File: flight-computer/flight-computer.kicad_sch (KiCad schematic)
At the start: 42 parts, among them J1 Screw_Terminal_01x02, J2 Screw_Terminal_01x02, U1 MPU6050, U2 BMP180, U3 ESP32_DEVKIT, U4 W25Q64FV_Winbond_Flash_Memory, U5 MPU6050, U6 W25Q64FV_Winbond_Flash_Memory, U7 MPU6050, U8 BMP180, U9 BMP180

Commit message: added NEO6M GPS footprint
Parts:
- added U10: GPS-NEO6M, custom-footprints:GPS-NEO6M, symbol modules:GPS-NEO6M
- gave numbers to parts that had none: 2
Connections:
- net +5V: now also U10.1 (VCC)
- net GND: now also U10.4 (GND)
- net GPS_TX: now reaches U3.29 (RX2)
- net GPS_TX: now also U10.3 (TX)
- net GPS_RX: now reaches U3.30 (TX2)
- net GPS_RX: now also U10.2 (RX)
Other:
- note added: "GPS Module"
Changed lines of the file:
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@@
     (stroke (width 0) (type default) (color 0 0 0 0))
   )
-  (polyline (pts (xy 130.175 145.415) (xy 130.175 38.735))
+  (polyline (pts (xy 130.175 118.745) (xy 130.175 56.515))
     (stroke (width 0) (type default) (color 0 0 0 0))
   )
@@
     (stroke (width 0) (type default) (color 0 0 0 0))
   )
+  (polyline (pts (xy 205.105 153.67) (xy 130.175 153.67))
+    (stroke (width 0) (type default) (color 0 0 0 0))
+  )
+  (wire (pts (xy 139.065 130.81) (xy 139.065 131.445))
+    (stroke (width 0) (type default) (color 0 0 0 0))
+  )
   (wire (pts (xy 43.18 165.1) (xy 57.785 165.1))
     (stroke (width 0) (type default) (color 0 0 0 0))
@@
     (stroke (width 0) (type default) (color 0 0 0 0))
   )
-  (polyline (pts (xy 205.74 38.735) (xy 130.175 38.735))
+  (polyline (pts (xy 205.74 56.515) (xy 130.175 56.515))
     (stroke (width 0) (type default) (color 0 0 0 0))
   )
@@
     (stroke (width 0) (type default) (color 0 0 0 0))
   )
-  (polyline (pts (xy 205.74 145.415) (xy 130.175 145.415))
+  (polyline (pts (xy 205.74 118.745) (xy 130.175 118.745))
     (stroke (width 0) (type default) (color 0 0 0 0))
   )
@@
     (stroke (width 0) (type default) (color 0 0 0 0))
   )
+  (polyline (pts (xy 205.105 123.19) (xy 205.105 153.67))
+    (stroke (width 0) (type default) (color 0 0 0 0))
+  )
   (wire (pts (xy 44.45 113.03) (xy 58.42 113.03))
     (stroke (width 0) (type default) (color 0 0 0 0))
   )
+  (polyline (pts (xy 130.175 123.19) (xy 130.175 153.67))
+    (stroke (width 0) (type default) (color 0 0 0 0))
+  )
   (wire (pts (xy 237.49 21.59) (xy 237.49 24.13))
     (stroke (width 0) (type default) (color 0 0 0 0))
@@
     (stroke (width 0) (type default) (color 0 0 0 0))
   )
+  (wire (pts (xy 159.385 130.81) (xy 139.065 130.81))
+    (stroke (width 0) (type default) (color 0 0 0 0))
+  )
   (polyline (pts (xy 127 153.035) (xy 127 105.41))
     (stroke (width 0) (type default) (color 0 0 0 0))
@@
     (stroke (width 0) (type default) (color 0 0 0 0))
   )
+  (wire (pts (xy 158.75 138.43) (xy 159.385 138.43))
+    (stroke (width 0) (type default) (color 0 0 0 0))
+  )
   (wire (pts (xy 40.005 33.655) (xy 40.005 38.1))
     (stroke (width 0) (type default) (color 0 0 0 0))
@@
     (stroke (width 0) (type default) (color 0 0 0 0))
   )
+  (polyline (pts (xy 130.175 123.19) (xy 205.105 123.19))
+    (stroke (width 0) (type default) (color 0 0 0 0))
+  )
   (wire (pts (xy 97.79 165.1) (xy 112.395 165.1))
     (stroke (width 0) (type default) (color 0 0 0 0))
@@
     (stroke (width 0) (type default) (color 0 0 0 0))
   )
-  (polyline (pts (xy 205.74 38.735) (xy 205.74 145.415))
+  (polyline (pts (xy 205.74 56.515) (xy 205.74 118.745))
     (stroke (width 0) (type default) (color 0 0 0 0))
   )
@@
     (stroke (width 0) (type default) (color 0 0 0 0))
   )
-  (text "MCU\n" (at 130.81 41.275 0)
+  (text "MCU\n" (at 130.81 59.69 0)
     (effects (font (size 1.27 1.27) bold) (justify left bottom))
   )
@@
     (at 76.2 109.855 0)
     (effects (font (size 1.27 1.27)) (justify left bottom))
+  )
+  (text "GPS Module" (at 130.81 125.73 0)
+    (effects (font (size 1.27 1.27) bold) (justify left bottom))
   )
   (text "Address: 0X77" (at 57.785 158.75 0)
@@
     )
   )
+  (global_label "GPS_RX" (shape input) (at 159.385 135.89 180) (fields_autoplaced)
+    (effects (font (size 1.27 1.27) bold) (justify right))
+    (property "Intersheet References" "${INTERSHEET_REFS}" (id 0) (at 149.5848 136.017 0)
+      (effects (font (size 1.27 1.27) bold) (justify right) hide)
+    )
+  )
   (global_label "~{HOLD}" (shape input) (at 247.65 57.15 0) (fields_autoplaced)
     (effects (font (size 1.27 1.27) bold) (justify left))
@@
     )
   )
+  (global_label "GPS_TX" (shape input) (at 186.055 90.805 0) (fields_autoplaced)
+    (effects (font (size 1.27 1.27) bold) (justify left))
+    (property "Intersheet References" "${INTERSHEET_REFS}" (id 0) (at 195.5528 90.932 0)
+      (effects (font (size 1.27 1.27) bold) (justify left) hide)
+    )
+  )
   (global_label "SDA" (shape input) (at 39.37 119.38 90) (fields_autoplaced)
     (effects (font (size 1.27 1.27)) (justify left))
@@
     )
   )
+  (global_label "GPS_TX" (shape input) (at 159.385 133.35 180) (fields_autoplaced)
+    (effects (font (size 1.27 1.27) bold) (justify right))
+    (property "Intersheet References" "${INTERSHEET_REFS}" (id 0) (at 149.8872 133.223 0)
+      (effects (font (size 1.27 1.27) bold) (justify right) hide)
+    )
+  )
   (global_label "D0" (shape input) (at 223.52 57.15 180) (fields_autoplaced)
     (effects (font (size 1.27 1.27) bold) (justify right))
@@
     (effects (font (size 1.27 1.27) bold) (justify left))
     (property "Intersheet References" "${INTERSHEET_REFS}" (id 0) (at 253.8216 60.833 0)
+      (effects (font (size 1.27 1.27) bold) (justify left) hide)
+    )
+  )
+  (global_label "GPS_RX" (shape input) (at 186.055 88.265 0) (fields_autoplaced)
+    (effects (font (size 1.27 1.27) bold) (justify left))
+    (property "Intersheet References" "${INTERSHEET_REFS}" (id 0) (at 195.8552 88.138 0)
       (effects (font (size 1.27 1.27) bold) (justify left) hide)
     )
@@
   (symbol (lib_id "power:GND") (at 62.865 47.625 0) (unit 1)
     (in_bom yes) (on_board yes)
-    (property "Reference" "#PWR?" (id 0) (at 62.865 53.975 0)
+    (property "Reference" "#PWR0141" (id 0) (at 62.865 53.975 0)
       (effects (font (size 1.27 1.27)) hide)
     )
@@
     )
     (property "Datasheet" "" (id 3) (at 62.865 47.625 0)
+      (effects (font (size 1.27 1.27)) hide)
+    )
+    (pin "1")
+  )
+  (symbol (lib_id "power:+5V") (at 158.75 138.43 90) (unit 1)
+    (in_bom yes) (on_board yes)
+    (property "Reference" "#PWR010" (id 0) (at 162.56 138.43 0)
+      (effects (font (size 1.27 1.27)) hide)
+    )
+    (property "Value" "+5V" (id 1) (at 151.765 138.43 90)
+      (effects (font (size 1.27 1.27)) (justify right))
+    )
+    (property "Footprint" "" (id 2) (at 158.75 138.43 0)
+      (effects (font (size 1.27 1.27)) hide)
+    )
+    (property "Datasheet" "" (id 3) (at 158.75 138.43 0)
       (effects (font (size 1.27 1.27)) hide)
     )
@@
     (pin "1")
   )
+  (symbol (lib_id "modules:GPS-NEO6M") (at 161.925 127 0) (unit 1)
+    (in_bom yes) (on_board yes) (fields_autoplaced)
+    (property "Reference" "U10" (id 0) (at 188.595 133.9849 0)
+      (effects (font (size 1.27 1.27)) (justify left))
+    )
+    (property "Value" "GPS-NEO6M" (id 1) (at 188.595 136.5249 0)
+      (effects (font (size 1.27 1.27)) (justify left))
+    )
+    (property "Footprint" "custom-footprints:GPS-NEO6M" (id 2) (at 168.275 125.73 0)
+      (effects (font (size 1.27 1.27)) hide)
+    )
+    (property "Datasheet" "" (id 3) (at 168.275 125.73 0)
+      (effects (font (size 1.27 1.27)) hide)
+    )
+    (pin "1")
+    (pin "2")
+    (pin "3")
+    (pin "4")
+  )
   (symbol (lib_id "power:GND") (at 261.62 66.04 0) (unit 1)
     (in_bom yes) (on_board yes)
@@
   (symbol (lib_id "Device:R") (at 62.865 43.815 0) (unit 1)
     (in_bom yes) (on_board yes) (fields_autoplaced)
-    (property "Reference" "R?" (id 0) (at 64.77 42.5449 0)
+    (property "Reference" "R1" (id 0) (at 64.77 42.5449 0)
       (effects (font (size 1.27 1.27)) (justify left))
     )
@@
   (symbol (lib_id "Device:LED") (at 62.865 36.195 90) (unit 1)
     (in_bom yes) (on_board yes) (fields_autoplaced)
-    (property "Reference" "D?" (id 0) (at 66.04 36.5124 90)
+    (property "Reference" "D2" (id 0) (at 66.04 36.5124 90)
       (effects (font (size 1.27 1.27)) (justify right))
     )
@@
     (pin "1")
   )
+  (symbol (lib_id "power:GND") (at 139.065 131.445 0) (unit 1)
+    (in_bom yes) (on_board yes)
+    (property "Reference" "#PWR09" (id 0) (at 139.065 137.795 0)
+      (effects (font (size 1.27 1.27)) hide)
+    )
+    (property "Value" "GND" (id 1) (at 138.43 135.89 0))
+    (property "Footprint" "" (id 2) (at 139.065 131.445 0)
+      (effects (font (size 1.27 1.27)) hide)
+    )
+    (property "Datasheet" "" (id 3) (at 139.065 131.445 0)
+      (effects (font (size 1.27 1.27)) hide)
+    )
+    (pin "1")
+  )
   (symbol (lib_id "toggle-switch:100SP1T1B4M2QE") (at 48.26 31.115 0) (unit 1)
     (in_bom yes) (on_board yes) (fields_autoplaced)
@@
       (reference "#PWR08") (unit 1) (value "GND") (footprint "")
     )
+    (path "/c8c902c7-0ab4-48a4-a0a1-d40b6bf4a2d5"
+      (reference "#PWR09") (unit 1) (value "GND") (footprint "")
+    )
+    (path "/2b471a04-e055-4567-a502-ae2af7a721d1"
+      (reference "#PWR010") (unit 1) (value "+5V") (footprint "")
+    )
     (path "/4fb3bb21-cae0-4e69-9248-759f3524059c"
       (reference "#PWR0101") (unit 1) (value "GND") (footprint "")
@@
     )
     (path "/23c0bb96-3ff8-4937-a107-4f0715059131"
-      (reference "#PWR?") (unit 1) (value "GND") (footprint "")
+      (reference "#PWR0141") (unit 1) (value "GND") (footprint "")
     )
     (path "/2dae9a2c-6370-4b32-88be-85d2eb9d4c00"
@@
     )
     (path "/68b26feb-598c-4a44-98ca-ad2ff34adbc9"
-      (reference "D?") (unit 1) (value "LED") (footprint "LED_SMD:LED_0805_2012Metric")
+      (reference "D2") (unit 1) (value "LED") (footprint "LED_SMD:LED_0805_2012Metric")
     )
     (path "/1936f0f3-1085-45ad-b499-8407ccaff28d"
@@
     )
     (path "/50759d54-4560-42cd-adb6-a64ce252b529"
-      (reference "R?") (unit 1) (value "R") (footprint "Resistor_SMD:R_0805_2012Metric")
+      (reference "R1") (unit 1) (value "R") (footprint "Resistor_SMD:R_0805_2012Metric")
     )
     (path "/cf0203bf-410f-4e09-a470-8e92c82dea6c"
@@
       (reference "U9") (unit 1) (value "BMP180") (footprint "custom-footprints:BMP180")
     )
-  )
+    (path "/4846449d-5e6e-4ab2-965e-226ba08fbd54"
+      (reference "U10") (unit 1) (value "GPS-NEO6M") (footprint "custom-footprints:GPS-NEO6M")
+    )
+  )

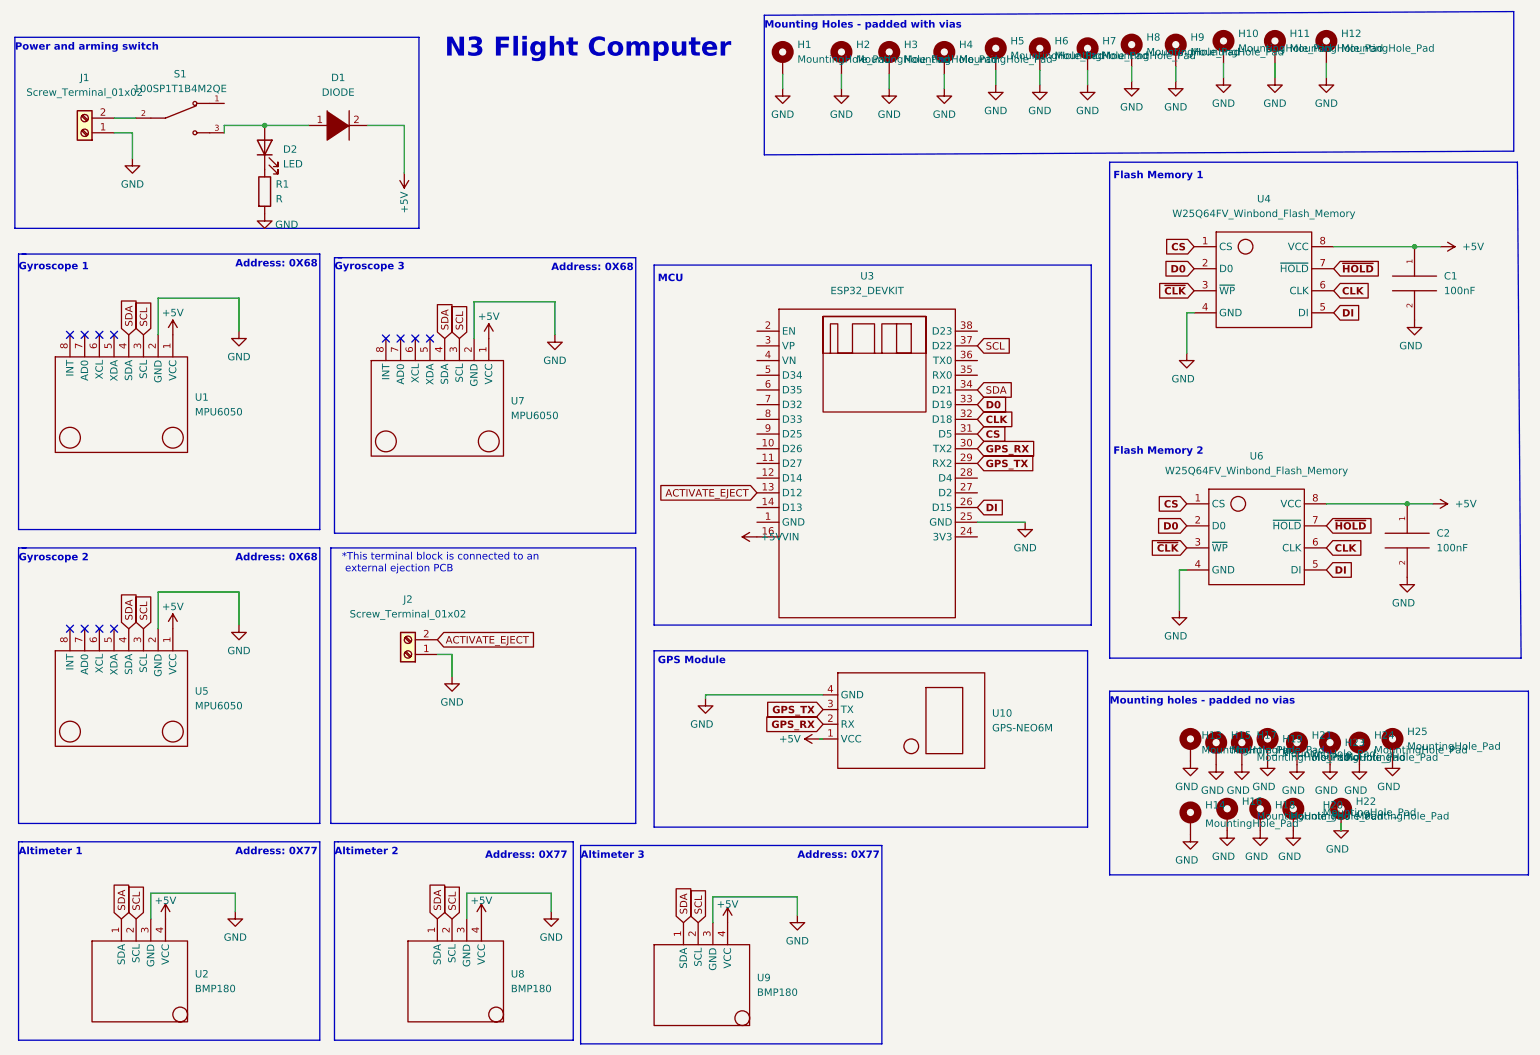
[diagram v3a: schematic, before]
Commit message: added pcb pdfs
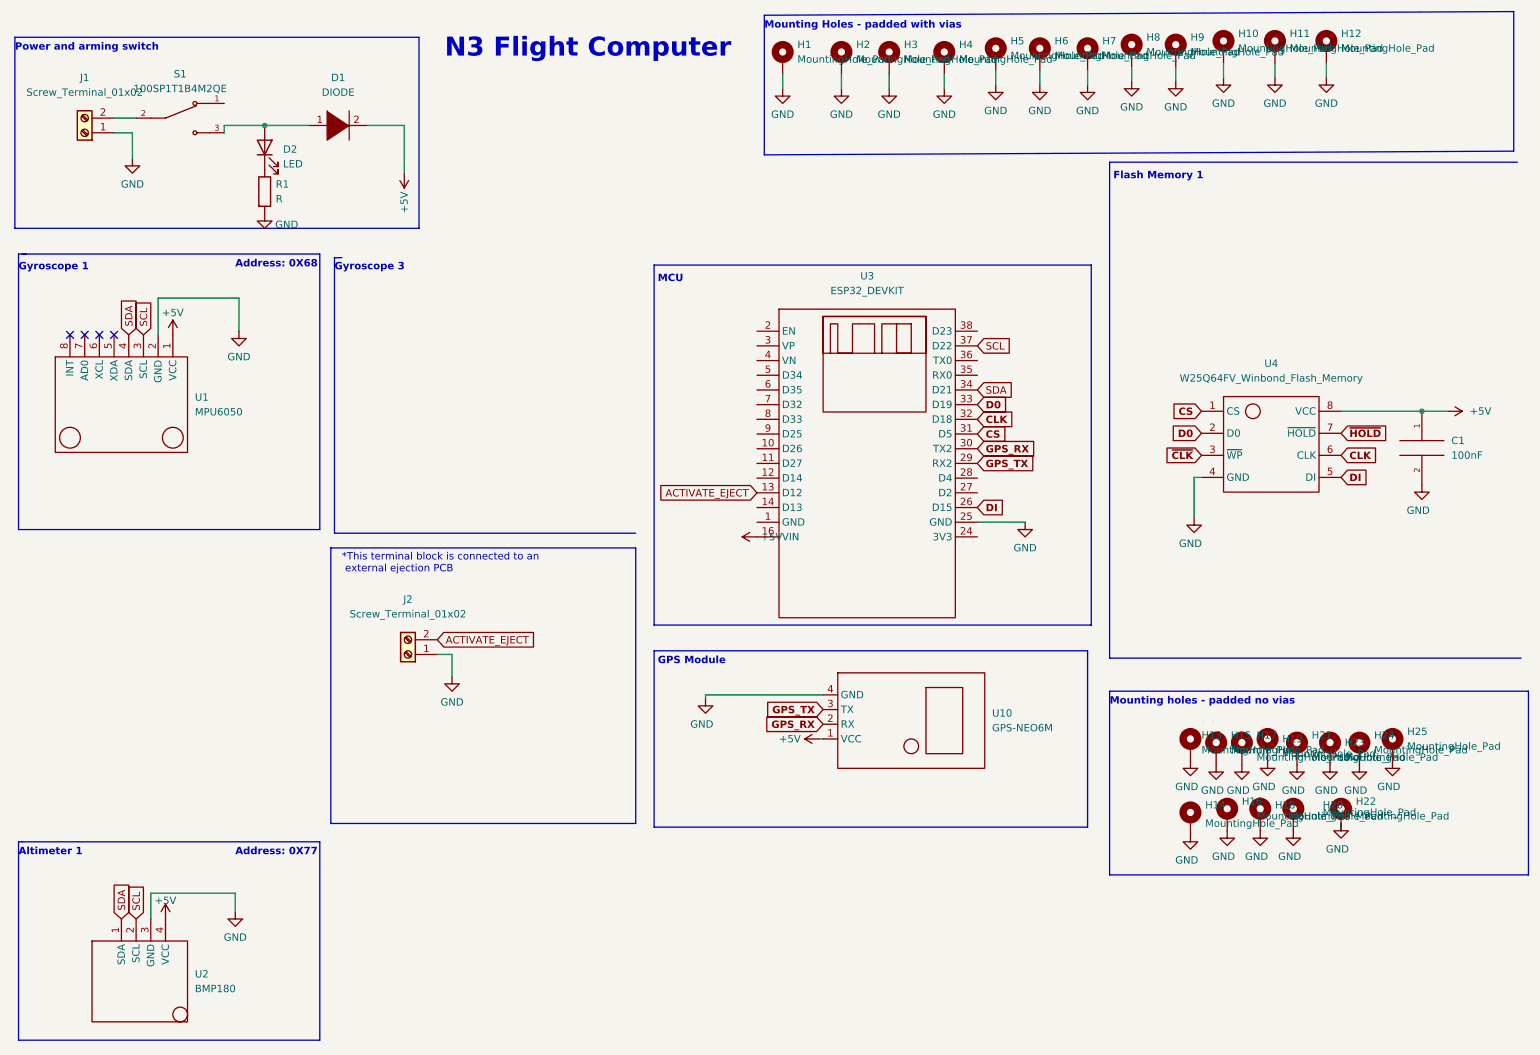
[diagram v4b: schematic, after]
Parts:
- removed C2: 100nF, Capacitor_SMD:C_0805_2012Metric, symbol pspice:CAP
- removed U5, U7: MPU6050, custom-footprints:MPU6050, symbol modules:MPU6050
- removed U6: W25Q64FV_Winbond_Flash_Memory, Package_SO:HTSOP-8-1EP_3.9x4.9mm_P1.27mm_EP2.4x3.2mm, symbol modules:W25Q64FV_Winbond_Flash_Memory
- removed U8, U9: BMP180, custom-footprints:BMP180, symbol modules:BMP180
- C1: footprint Capacitor_SMD:C_0805_2012Metric -> Capacitor_THT:CP_Radial_D4.0mm_P1.50mm
- D2: footprint LED_SMD:LED_0805_2012Metric -> LED_THT:LED_D3.0mm
- R1: footprint Resistor_SMD:R_0805_2012Metric -> Resistor_THT:R_Axial_DIN0204_L3.6mm_D1.6mm_P7.62mm_Horizontal
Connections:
- no-connect marks 12 -> 4
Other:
- note removed: "Altimeter 2"
- note removed: "Altimeter 3"
- note removed: "Flash Memory 2"
- note removed: "Gyroscope 2"
- moved on the sheet: C1, U4
